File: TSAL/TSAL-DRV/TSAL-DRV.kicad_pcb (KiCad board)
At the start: 2 copper layers, 42.5 x 42.5 mm, 23 parts, among them J1 Conn_01x08_Male, J2 Conn_01x03_Male, Q1 IRF9540N, Q2 IRF540N, U1 NE555

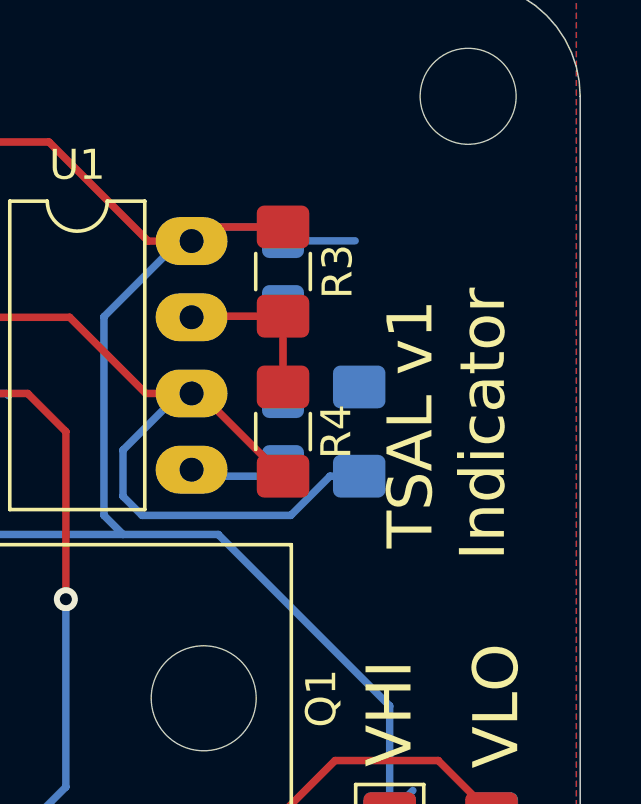
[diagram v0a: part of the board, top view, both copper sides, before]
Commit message: Aesthetic upgrades to schematic, render
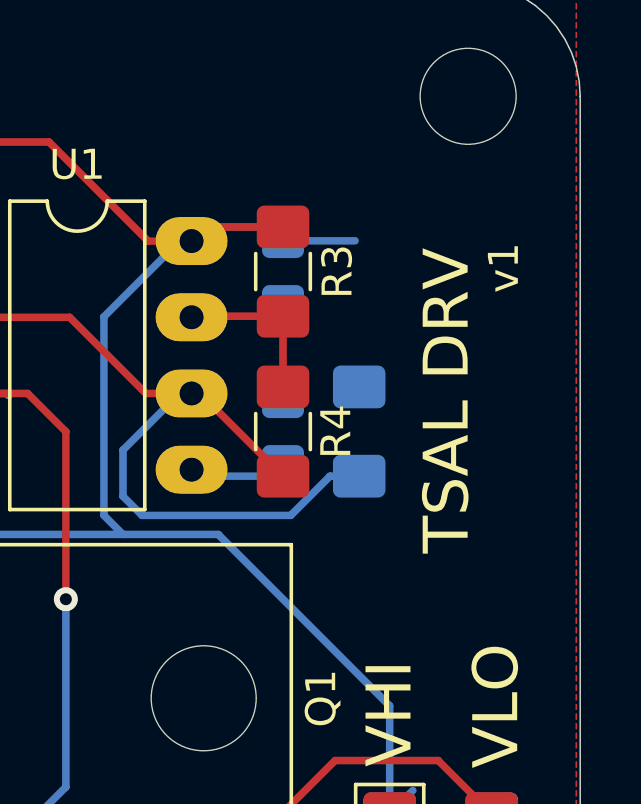
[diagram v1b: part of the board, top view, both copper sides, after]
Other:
- board text added: "TSAL DRV"
- board text added: "v1"
- board text removed: "TSAL v1 Indicator"
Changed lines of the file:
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@@
   (general
     (thickness 1.6)
-    (drawings 12)
+    (drawings 13)
     (tracks 121)
     (zones 0)
@@
     )
   )
+  (gr_text v1 (at 123.825 47.625 90) (layer F.SilkS)
+    (effects (font (size 1 1) (thickness 0.25)))
+  )
   (gr_line (start 83.82 76.835) (end 83.82 41.91) (layer Edge.Cuts) (width 0.05))
   (gr_line (start 122.555 80.645) (end 87.63 80.645) (layer Edge.Cuts) (width 0.05))
@@
     (effects (font (size 1 1) (thickness 0.15)))
   )
-  (gr_text "TSAL v1\nIndicator" (at 121.92 52.832 90) (layer F.SilkS)
-    (effects (font (size 1.5 1.5) (thickness 0.3)))
+  (gr_text "TSAL DRV" (at 121.92 57.15 90) (layer F.SilkS)
+    (effects (font (size 1.5 1.5) (thickness 0.3)) (justify left))
   )
   (gr_text VHI (at 120.015 62.484 90) (layer F.SilkS)

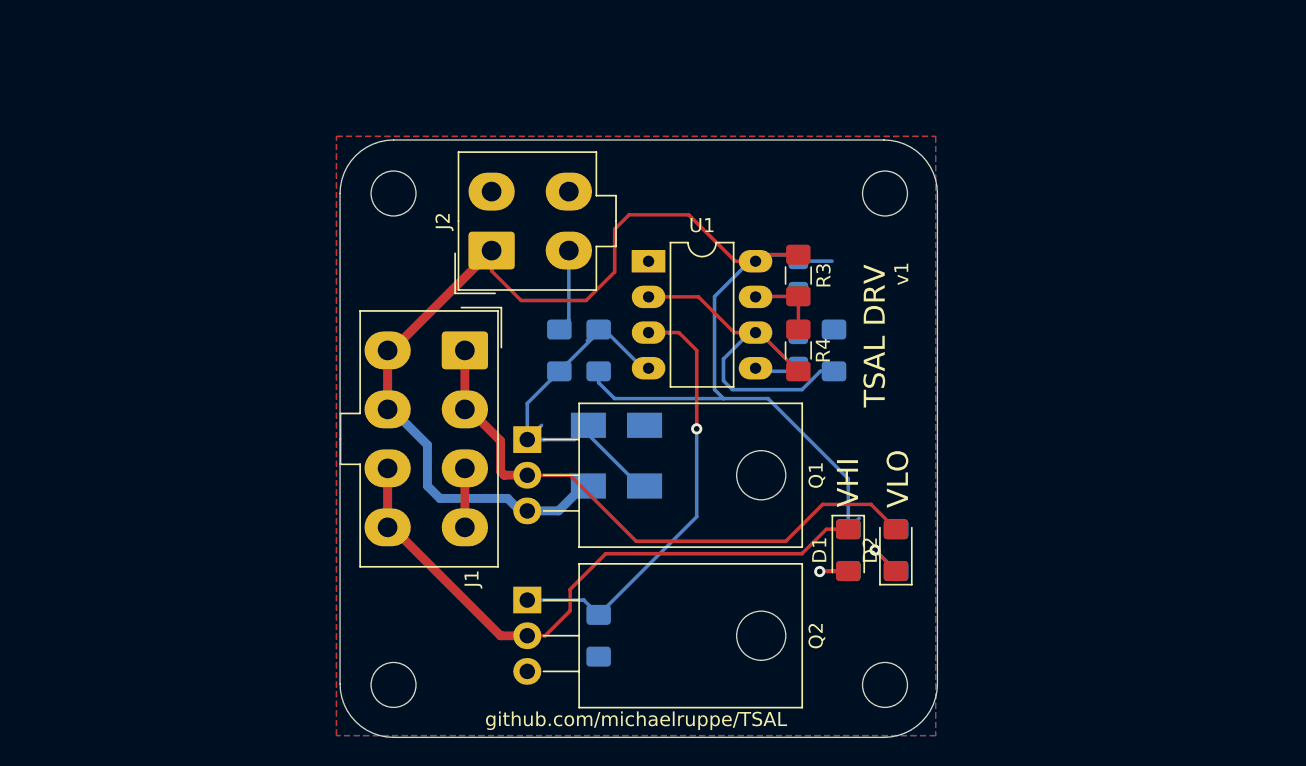
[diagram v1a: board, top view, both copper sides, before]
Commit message: Update TSAL-DRV to v2 schematic and select parts. Need route board
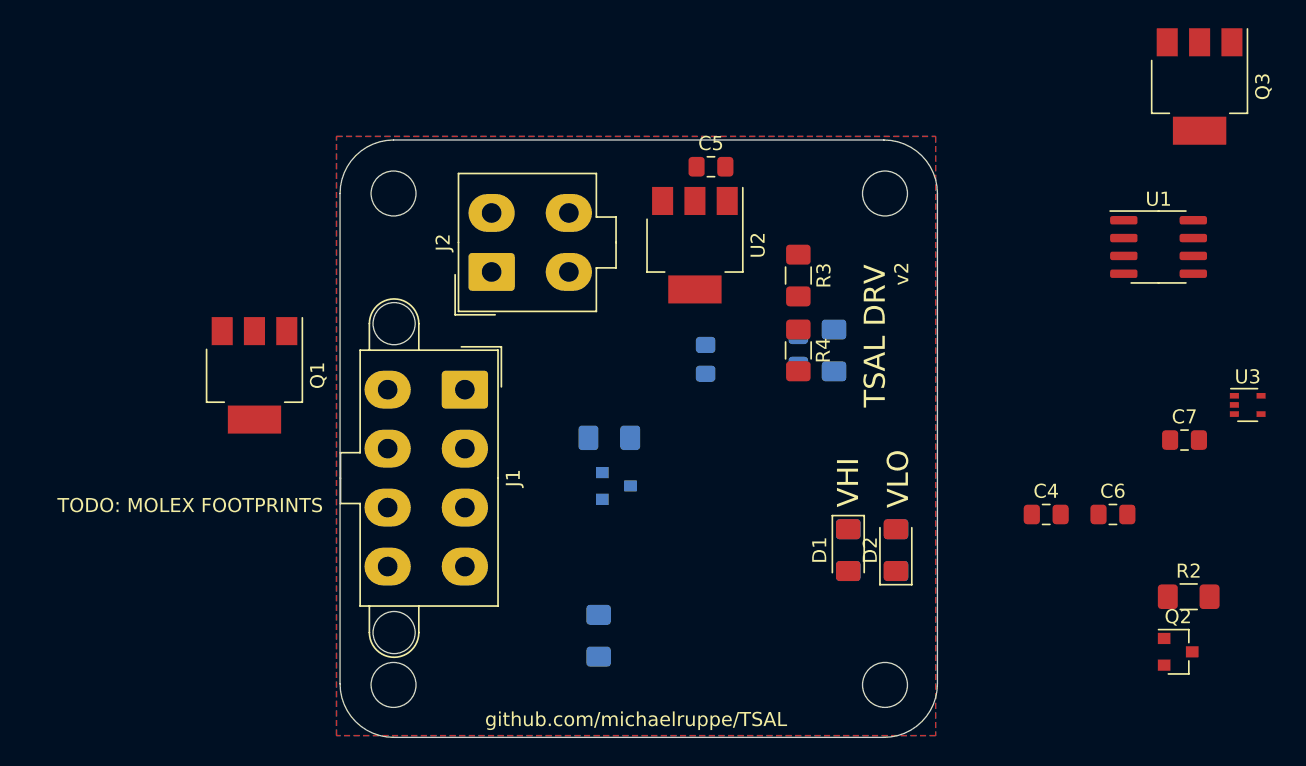
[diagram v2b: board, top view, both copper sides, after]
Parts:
- removed D4: NRVA4004T3G, Diode_SMD:D_SMA
- added C4: 1u, Capacitor_SMD:C_0805_2012Metric_Pad1.15x1.40mm_HandSolder, F.Cu at (134.1, 64.8)
- added C5: 1u, Capacitor_SMD:C_0805_2012Metric_Pad1.15x1.40mm_HandSolder, F.Cu at (110.2, 40.0)
- added C6: 100n, Capacitor_SMD:C_0805_2012Metric_Pad1.15x1.40mm_HandSolder, F.Cu at (138.9, 64.8)
- added C7: 10n, Capacitor_SMD:C_0805_2012Metric_Pad1.15x1.40mm_HandSolder, F.Cu at (144.0, 59.5)
- added Q3: MCT06P10-TP, Package_TO_SOT_SMD:SOT-223-3_TabPin2, F.Cu at (145.0, 34.3)
- added U2: AMS1117-5.0, Package_TO_SOT_SMD:SOT-223-3_TabPin2, F.Cu at (109.1, 45.6)
- added U3: 74LVC1G17, Package_TO_SOT_SMD:SOT-353_SC-70-5, F.Cu at (148.5, 57.0)
- D3: value NRVA4004T3G -> BZX84C5V1; footprint Diode_SMD:D_SMA -> Diode_SMD:D_SOT-23_ANK
- J1: footprint Connector_Molex:Molex_Mini-Fit_Jr_5566-08A_2x04_P4.20mm_Vertical -> Connector_Molex:Molex_Mini-Fit_Jr_5566-08A2_2x04_P4.20mm_Vertical
- Q1: value IRF9540N -> MCT06P10-TP; footprint Package_TO_SOT_THT:TO-220-3_Horizontal_TabDown -> Package_TO_SOT_SMD:SOT-223-3_TabPin2
- Q2: value IRF540N -> 2N7002; footprint Package_TO_SOT_THT:TO-220-3_Horizontal_TabDown -> Package_TO_SOT_SMD:SOT-23
- R1: value 220 -> 2k2
- R2: value 22k -> 220k; moved to F.Cu
- U1: footprint Package_DIP:DIP-8_W7.62mm_LongPads -> Package_SO:SOIC-8_3.9x4.9mm_P1.27mm
- moved Q2 46.5 mm to (143.5, 74.5), turned to 0 degrees
- moved R2 45.5 mm to (144.3, 70.6), turned to 0 degrees
- moved U1 36.3 mm to (142.1, 45.7)
- moved Q1 20.0 mm to (77.7, 54.9)
- moved C1 8.90 mm to (109.9, 53.7)
- moved R1 7.17 mm to (103.0, 59.3), turned to 180 degrees
- moved J1 2.79 mm to (92.7, 55.9)
- moved J2 1.52 mm to (94.6, 47.5)
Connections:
- C1 pad 1: +12V -> +5V
- D1 pad 1: RED- -> GND
- D3 pad 1: +12V -> Net-(C7-Pad1)
- D3 pad 2: Net-(D3-Pad2) -> GND
- J1 pad 5: +12V -> RED+
- J1 pad 6: +12V -> RED+
- J1 pad 7: RED- -> GND
- J1 pad 8: RED- -> GND
- Q1 pad 1: Net-(D3-Pad2) -> Net-(Q1-Pad1)
- Q2 pad 2: RED- -> GND
- Q2 pad 3: GND -> Net-(Q2-Pad3)
- R1 pad 1: Net-(D3-Pad2) -> Net-(C7-Pad1)
- R2 pad 1: +12V -> +5V
- R2 pad 2: Net-(D3-Pad2) -> Net-(Q2-Pad3)
- R3 pad 1: +12V -> +5V
- R6 pad 1: +12V -> RED+
- U1 pad 4: Net-(D3-Pad2) -> Net-(Q1-Pad1)
- U1 pad 8: +12V -> +5V
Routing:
- net +12V: track 107.6 -> 0.00 mm
- net RED-: track 44.6 -> 0.00 mm
- net GRN+: track 41.9 -> 0.00 mm
- net Net-(Q2-Pad1): track 32.8 -> 0.00 mm, vias 1 -> 0
- net Net-(D3-Pad2): track 29.4 -> 0.00 mm
- net Net-(C3-Pad1): track 26.6 -> 0.00 mm
- net /VHI: track 5.90 -> 0.00 mm
- net Net-(R3-Pad2): track 5.42 -> 0.00 mm
- net Net-(D2-Pad1): track 4.22 -> 0.00 mm, vias 1 -> 0
- net GND: track 4.20 -> 0.00 mm
- net Net-(D1-Pad2): track 4.09 -> 0.00 mm, vias 1 -> 0
- net Net-(C2-Pad1): track 3.14 -> 0.00 mm
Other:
- board text added: "TODO: MOLEX FOOTPRINTS"
- board text added: "v2"
- board text removed: "v1"

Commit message: Update TSAL versioning, renders and schematic prints
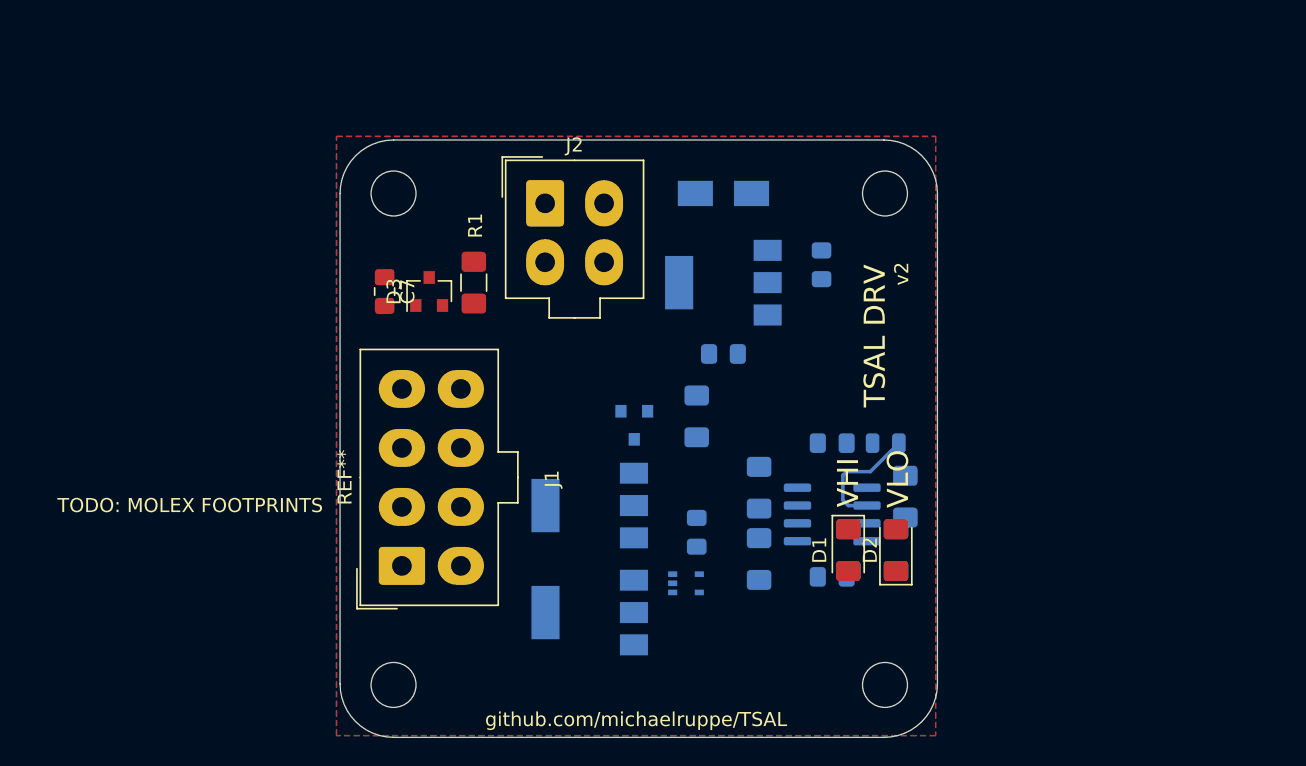
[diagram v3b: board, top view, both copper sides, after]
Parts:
- added D4: D, Diode_SMD:D_SMA, B.Cu at (111.1, 41.9)
- C3: footprint Capacitor_SMD:C_1206_3216Metric_Pad1.42x1.75mm_HandSolder -> Capacitor_SMD:C_0805_2012Metric
- C4, C5, C6, Q1, Q2, Q3, R2, R3, R4, U1, U2, U3: moved to B.Cu
- D3, R1: moved to F.Cu
- J1: footprint Connector_Molex:Molex_Mini-Fit_Jr_5566-08A2_2x04_P4.20mm_Vertical -> Mini-Fit-Jr-4.20mm-pitch:Molex-Mini-Fit-Jr-8-pin-P4.2mm-RowP4.2mm
- J2: footprint Connector_Molex:Molex_Mini-Fit_Jr_5566-04A_2x02_P4.20mm_Vertical -> Mini-Fit-Jr-4.20mm-pitch:Molex-Mini-Fit-Jr-4-pin-P4.2mm-RowP4.2mm
- moved C7 57.9 mm to (87.0, 48.9), turned to 270 degrees
- moved Q3 52.7 mm to (101.6, 64.1), turned to 180 degrees
- moved U3 42.0 mm to (108.5, 69.7)
- moved Q2 42.0 mm to (104.8, 58.4), turned to 270 degrees
- moved R2 37.3 mm to (109.2, 57.8), turned to 270 degrees
- moved U1 30.1 mm to (118.9, 64.8), turned to 180 degrees
- moved C6 29.7 mm to (109.2, 66.0), turned to 90 degrees
- moved Q1 29.2 mm to (101.6, 71.8), turned to 180 degrees
- moved R5 24.0 mm to (124.1, 63.5), turned to 90 degrees
- moved C4 23.9 mm to (118.1, 47.0), turned to 90 degrees
- moved D3 19.2 mm to (90.2, 48.9), turned to 90 degrees
- moved C2 16.3 mm to (118.9, 69.2), turned to 0 degrees
- moved R3 15.4 mm to (113.7, 62.9)
- moved R4 15.1 mm to (113.7, 67.9)
- moved R1 14.7 mm to (93.3, 48.3), turned to 90 degrees
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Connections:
- C4 pad 1: +12V -> Net-(C4-Pad1)
- U2 pad 3: +12V -> Net-(C4-Pad1)
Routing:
- net Net-(C3-Pad1): track 0.00 -> 8.58 mm
